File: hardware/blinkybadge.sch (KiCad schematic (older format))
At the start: 21 parts, among them IC101 ATMEGA8U2, P101 USB_OTG, P102 CONN_02X03, Q101 Q_PMOS_GDS, SW101 SPST, U101 ATECC508A, Y101 16MHz

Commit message: Layout complete
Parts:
- added R105: DNP, Resistors_SMD:R_0603, symbol R
- added W3: HWBE, Measurement_Points:Measurement_Point_Round-SMD-Pad_Small, symbol TEST_1P
- P102: footprint (none) -> lib:CONN_2.54mm_2x3_TP
- renumbered W3 to W4
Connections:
- net VCC: now also R105.1
- net at IC101.10 ((INT5/AIN3)PD4): now also C105.1, R104.2
- net at IC101.11 ((XCK/AIN4/PCINT12)PD5): now also C105.2
- net at IC101.13 ((~CTS~/~HWB~/AIN6/T0/INT7)PD7): now also R105.2, W3.1
- net at IC101.26 ((PCINT10)PC4): no longer C105.2
- now unconnected: IC101.5 ((PCINT11/AIN2)PC2)
- no-connect marks 2 -> 12
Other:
- moved on the sheet: C105, R104, W4
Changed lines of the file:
@@
 L C C105
 U 1 1 577EF93B
-P 7050 5150
-F 0 "C105" H 7075 5250 50  0000 L CNN
-F 1 "C" H 7075 5050 50  0000 L CNN
-F 2 "Capacitors_SMD:C_0603" H 7088 5000 50  0001 C CNN
-F 3 "" H 7050 5150 50  0000 C CNN
-	1    7050 5150
+P 7050 4650
+F 0 "C105" H 7075 4750 50  0000 L CNN
+F 1 "C" H 7075 4550 50  0000 L CNN
+F 2 "Capacitors_SMD:C_0603" H 7088 4500 50  0001 C CNN
+F 3 "" H 7050 4650 50  0000 C CNN
+	1    7050 4650
 	0    1    1    0
 $EndComp
@@
 L R R104
 U 1 1 577EF9C0
-P 7450 5050
-F 0 "R104" V 7530 5050 50  0000 C CNN
-F 1 "R" V 7450 5050 50  0000 C CNN
-F 2 "Resistors_SMD:R_0603" V 7380 5050 50  0001 C CNN
-F 3 "" H 7450 5050 50  0000 C CNN
-	1    7450 5050
+P 7450 4550
+F 0 "R104" V 7530 4550 50  0000 C CNN
+F 1 "R" V 7450 4550 50  0000 C CNN
+F 2 "Resistors_SMD:R_0603" V 7380 4550 50  0001 C CNN
+F 3 "" H 7450 4550 50  0000 C CNN
+	1    7450 4550
 	0    1    1    0
 $EndComp
@@
 F 0 "P102" H 7450 2850 50  0000 C CNN
 F 1 "CONN_02X03" H 7450 2450 50  0000 C CNN
-F 2 "" H 7450 1450 50  0001 C CNN
+F 2 "lib:CONN_2.54mm_2x3_TP" H 7450 1450 50  0001 C CNN
 F 3 "" H 7450 1450 50  0000 C CNN
 	1    7450 2650
@@
 	1600 2400 1600 2600
 Wire Wire Line
-	1500 2000 1950 2000
-Wire Wire Line
-	1950 2000 2300 2000
+	1500 2000 2300 2000
 Wire Wire Line
 	3350 2000 3000 2000
@@
 	5100 1600 5100 1700
 Wire Wire Line
-	1950 1600 4400 1600
-Wire Wire Line
-	4400 1600 5100 1600
-Wire Wire Line
-	5100 1600 5500 1600
+	1950 1600 5500 1600
 Wire Wire Line
 	1950 1600 1950 2000
@@
 Connection ~ 5100 1600
 Wire Wire Line
-	5300 2000 5500 2000
-Wire Wire Line
-	5500 2000 5700 2000
-Wire Wire Line
-	5700 1700 5700 2000
-Wire Wire Line
-	5700 2000 5700 2850
-Wire Wire Line
-	5700 2850 5700 2950
+	5300 2000 5700 2000
 Connection ~ 5500 2000
 Wire Wire Line
@@
 	4400 4550 4400 5000
 Wire Wire Line
-	4400 5300 4400 5350
-Wire Wire Line
-	4400 5350 4400 5400
+	4400 5300 4400 5400
 Wire Wire Line
 	4600 4950 4600 5350
@@
 Connection ~ 4400 5350
 Wire Wire Line
-	4000 4050 4200 4050
-Wire Wire Line
-	4200 4050 4400 4050
+	4000 4050 4400 4050
 Wire Wire Line
 	4400 3850 4600 3850
@@
 	4400 3750 4400 3850
 Wire Wire Line
-	4000 3750 4200 3750
-Wire Wire Line
-	4200 3750 4400 3750
+	4000 3750 4400 3750
 Wire Wire Line
 	4600 3950 4400 3950
@@
 	3700 3750 3550 3750
 Wire Wire Line
-	3550 3750 3550 4050
-Wire Wire Line
-	3550 4050 3550 4200
+	3550 3750 3550 4200
 Connection ~ 3550 4050
 Wire Wire Line
@@
 	8000 3750 8000 3850
 Wire Wire Line
-	7900 3650 8000 3650
-Wire Wire Line
 	8000 3650 8000 3550
 Wire Wire Line
-	4150 2850 4500 2850
-Wire Wire Line
-	4500 2850 5700 2850
-Wire Wire Line
-	4500 2850 4500 3750
-Wire Wire Line
-	4500 3750 4500 4650
+	5700 2850 4150 2850
+Wire Wire Line
+	4500 2850 4500 4650
 Wire Wire Line
 	4500 3750 4600 3750
@@
 	8950 4150 9100 4150
 Wire Wire Line
-	6800 5050 7250 5050
-Wire Wire Line
-	7250 5050 7300 5050
-Wire Wire Line
-	6800 5150 6900 5150
-Wire Wire Line
-	7200 5150 7250 5150
-Wire Wire Line
-	7250 5150 7250 5050
-Connection ~ 7250 5050
-Wire Wire Line
-	7600 5050 7850 5050
+	6800 4550 7300 4550
+Wire Wire Line
+	6800 4650 6900 4650
+Wire Wire Line
+	7200 4650 7250 4650
+Wire Wire Line
+	7250 4650 7250 4550
+Connection ~ 7250 4550
+Wire Wire Line
+	7600 4550 7850 4550
 Wire Wire Line
 	4600 2750 7200 2750
@@
 	6800 4450 6950 4450
 $Comp
-L TEST_1P W3
+L TEST_1P W4
 U 1 1 57805F3E
-P 7850 5050
-F 0 "W3" H 7850 5320 50  0000 C CNN
-F 1 "CAP_SENSE_BUTTON" H 7850 5250 50  0000 C CNN
-F 2 "Measurement_Points:Measurement_Point_Round-SMD-Pad_Small" H 8050 5050 50  0001 C CNN
-F 3 "" H 8050 5050 50  0000 C CNN
-	1    7850 5050
+P 7850 4550
+F 0 "W4" H 7850 4820 50  0000 C CNN
+F 1 "CAP_SENSE_BUTTON" H 7850 4750 50  0000 C CNN
+F 2 "Measurement_Points:Measurement_Point_Round-SMD-Pad_Small" H 8050 4550 50  0001 C CNN
+F 3 "" H 8050 4550 50  0000 C CNN
+	1    7850 4550
 	1    0    0    -1
 $EndComp
@@
 Text Label 4000 4850 0    60   ~ 0
 USBR_N
+$Comp
+L TEST_1P W3
+U 1 1 57845845
+P 7600 4850
+F 0 "W3" H 7600 5120 50  0000 C CNN
+F 1 "HWBE" H 7600 5050 50  0000 C CNN
+F 2 "Measurement_Points:Measurement_Point_Round-SMD-Pad_Small" H 7800 4850 50  0001 C CNN
+F 3 "" H 7800 4850 50  0000 C CNN
+	1    7600 4850
+	0    1    1    0
+$EndComp
+Wire Wire Line
+	6800 4850 7600 4850
+$Comp
+L R R105
+U 1 1 57846CBE
+P 7750 4650
+F 0 "R105" V 7830 4650 50  0000 C CNN
+F 1 "DNP" V 7750 4650 50  0000 C CNN
+F 2 "Resistors_SMD:R_0603" V 7680 4650 50  0001 C CNN
+F 3 "" H 7750 4650 50  0000 C CNN
+	1    7750 4650
+	0    1    1    0
+$EndComp
+Wire Wire Line
+	7600 4650 7450 4650
+Wire Wire Line
+	7450 4650 7450 4850
+Connection ~ 7450 4850
+Wire Wire Line
+	7900 4650 8000 4650
+Wire Wire Line
+	8000 4650 8000 4500
+$Comp
+L VCC #PWR013
+U 1 1 57846ECD
+P 8000 4500
+F 0 "#PWR013" H 8000 4350 50  0001 C CNN
+F 1 "VCC" H 8000 4650 50  0000 C CNN
+F 2 "" H 8000 4500 50  0000 C CNN
+F 3 "" H 8000 4500 50  0000 C CNN
+	1    8000 4500
+	1    0    0    -1
+$EndComp
+NoConn ~ 6800 3250
+NoConn ~ 6800 3850
+NoConn ~ 6800 3950
+NoConn ~ 6800 4250
+NoConn ~ 6800 5050
+NoConn ~ 6800 5150
+NoConn ~ 6800 5250
+NoConn ~ 6800 5350
+NoConn ~ 6800 5450
+NoConn ~ 6800 4750
+Wire Wire Line
+	7900 3650 8000 3650
+Wire Wire Line
+	5700 1700 5700 2950
 $EndSCHEMATC

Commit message: Add some layout tweaks
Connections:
- net STAT: now also IC101.12 ((~RTS~/AIN5/INT6)PD6)
- no-connect marks 12 -> 11
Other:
- moved on the sheet: C105, R104, R105, W3, W4
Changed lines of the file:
@@
 L C C105
 U 1 1 577EF93B
-P 7050 4650
-F 0 "C105" H 7075 4750 50  0000 L CNN
-F 1 "C" H 7075 4550 50  0000 L CNN
-F 2 "Capacitors_SMD:C_0603" H 7088 4500 50  0001 C CNN
-F 3 "" H 7050 4650 50  0000 C CNN
-	1    7050 4650
+P 7200 4650
+F 0 "C105" H 7225 4750 50  0000 L CNN
+F 1 "C" H 7225 4550 50  0000 L CNN
+F 2 "Capacitors_SMD:C_0603" H 7238 4500 50  0001 C CNN
+F 3 "" H 7200 4650 50  0000 C CNN
+	1    7200 4650
 	0    1    1    0
 $EndComp
@@
 L R R104
 U 1 1 577EF9C0
-P 7450 4550
-F 0 "R104" V 7530 4550 50  0000 C CNN
-F 1 "R" V 7450 4550 50  0000 C CNN
-F 2 "Resistors_SMD:R_0603" V 7380 4550 50  0001 C CNN
-F 3 "" H 7450 4550 50  0000 C CNN
-	1    7450 4550
+P 7600 4550
+F 0 "R104" V 7680 4550 50  0000 C CNN
+F 1 "R" V 7600 4550 50  0000 C CNN
+F 2 "Resistors_SMD:R_0603" V 7530 4550 50  0001 C CNN
+F 3 "" H 7600 4550 50  0000 C CNN
+	1    7600 4550
 	0    1    1    0
 $EndComp
@@
 	8950 4150 9100 4150
 Wire Wire Line
-	6800 4550 7300 4550
-Wire Wire Line
-	6800 4650 6900 4650
-Wire Wire Line
-	7200 4650 7250 4650
-Wire Wire Line
-	7250 4650 7250 4550
-Connection ~ 7250 4550
-Wire Wire Line
-	7600 4550 7850 4550
+	6800 4550 7450 4550
+Wire Wire Line
+	6800 4650 7050 4650
+Wire Wire Line
+	7350 4650 7400 4650
+Wire Wire Line
+	7400 4650 7400 4550
+Connection ~ 7400 4550
+Wire Wire Line
+	7750 4550 8000 4550
 Wire Wire Line
 	4600 2750 7200 2750
@@
 L TEST_1P W4
 U 1 1 57805F3E
-P 7850 4550
-F 0 "W4" H 7850 4820 50  0000 C CNN
-F 1 "CAP_SENSE_BUTTON" H 7850 4750 50  0000 C CNN
-F 2 "Measurement_Points:Measurement_Point_Round-SMD-Pad_Small" H 8050 4550 50  0001 C CNN
-F 3 "" H 8050 4550 50  0000 C CNN
-	1    7850 4550
+P 8000 4550
+F 0 "W4" H 8000 4820 50  0000 C CNN
+F 1 "CAP_SENSE_BUTTON" H 8000 4750 50  0000 C CNN
+F 2 "Measurement_Points:Measurement_Point_Round-SMD-Pad_Small" H 8200 4550 50  0001 C CNN
+F 3 "" H 8200 4550 50  0000 C CNN
+	1    8000 4550
 	1    0    0    -1
 $EndComp
@@
 L TEST_1P W3
 U 1 1 57845845
-P 7600 4850
-F 0 "W3" H 7600 5120 50  0000 C CNN
-F 1 "HWBE" H 7600 5050 50  0000 C CNN
-F 2 "Measurement_Points:Measurement_Point_Round-SMD-Pad_Small" H 7800 4850 50  0001 C CNN
-F 3 "" H 7800 4850 50  0000 C CNN
-	1    7600 4850
-	0    1    1    0
-$EndComp
-Wire Wire Line
-	6800 4850 7600 4850
+P 7750 4850
+F 0 "W3" H 7750 5120 50  0000 C CNN
+F 1 "HWBE" H 7750 5050 50  0000 C CNN
+F 2 "Measurement_Points:Measurement_Point_Round-SMD-Pad_Small" H 7950 4850 50  0001 C CNN
+F 3 "" H 7950 4850 50  0000 C CNN
+	1    7750 4850
+	0    1    1    0
+$EndComp
+Wire Wire Line
+	6800 4850 7750 4850
 $Comp
 L R R105
 U 1 1 57846CBE
-P 7750 4650
-F 0 "R105" V 7830 4650 50  0000 C CNN
-F 1 "DNP" V 7750 4650 50  0000 C CNN
-F 2 "Resistors_SMD:R_0603" V 7680 4650 50  0001 C CNN
-F 3 "" H 7750 4650 50  0000 C CNN
-	1    7750 4650
-	0    1    1    0
-$EndComp
-Wire Wire Line
-	7600 4650 7450 4650
-Wire Wire Line
-	7450 4650 7450 4850
-Connection ~ 7450 4850
-Wire Wire Line
-	7900 4650 8000 4650
-Wire Wire Line
-	8000 4650 8000 4500
+P 7900 4650
+F 0 "R105" V 7980 4650 50  0000 C CNN
+F 1 "DNP" V 7900 4650 50  0000 C CNN
+F 2 "Resistors_SMD:R_0603" V 7830 4650 50  0001 C CNN
+F 3 "" H 7900 4650 50  0000 C CNN
+	1    7900 4650
+	0    1    1    0
+$EndComp
+Wire Wire Line
+	7750 4650 7600 4650
+Wire Wire Line
+	7600 4650 7600 4850
+Connection ~ 7600 4850
+Wire Wire Line
+	8050 4650 8150 4650
+Wire Wire Line
+	8150 4650 8150 4500
 $Comp
 L VCC #PWR013
 U 1 1 57846ECD
-P 8000 4500
-F 0 "#PWR013" H 8000 4350 50  0001 C CNN
-F 1 "VCC" H 8000 4650 50  0000 C CNN
-F 2 "" H 8000 4500 50  0000 C CNN
-F 3 "" H 8000 4500 50  0000 C CNN
-	1    8000 4500
+P 8150 4500
+F 0 "#PWR013" H 8150 4350 50  0001 C CNN
+F 1 "VCC" H 8150 4650 50  0000 C CNN
+F 2 "" H 8150 4500 50  0000 C CNN
+F 3 "" H 8150 4500 50  0000 C CNN
+	1    8150 4500
 	1    0    0    -1
 $EndComp
@@
 NoConn ~ 6800 5350
 NoConn ~ 6800 5450
-NoConn ~ 6800 4750
 Wire Wire Line
 	7900 3650 8000 3650
 Wire Wire Line
 	5700 1700 5700 2950
+Wire Wire Line
+	6800 4750 7050 4750
+Text Label 6850 4750 0    60   ~ 0
+STAT
 $EndSCHEMATC

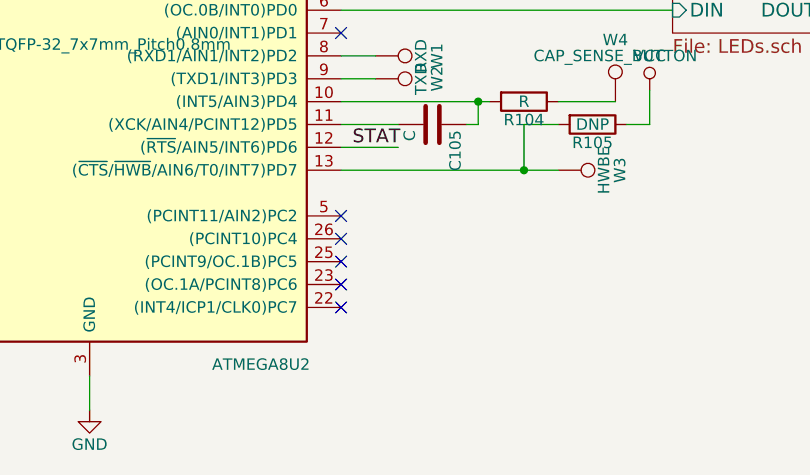
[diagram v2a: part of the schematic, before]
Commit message: Add footprints and the EURion constellations
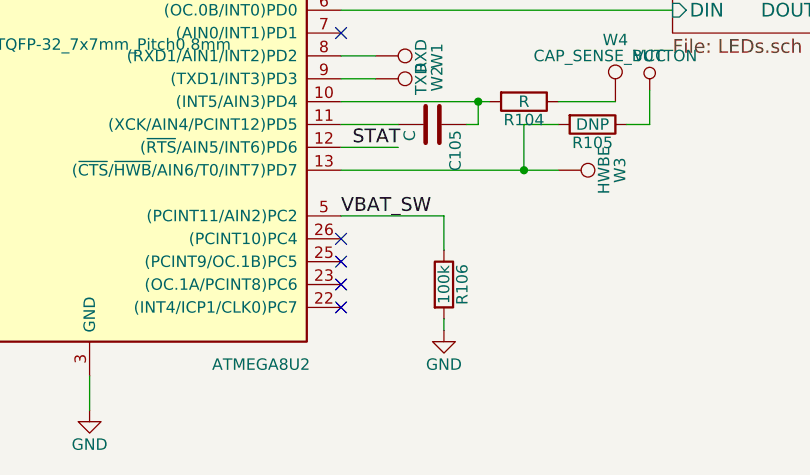
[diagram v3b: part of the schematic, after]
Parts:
- added R106: 100k, Resistors_SMD:R_0603, symbol R
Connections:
- net GND: now also R106.2
- net VBAT_SW: now also IC101.5 ((PCINT11/AIN2)PC2), R106.1
- no-connect marks 11 -> 10
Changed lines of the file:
@@
 NoConn ~ 6800 3950
 NoConn ~ 6800 4250
-NoConn ~ 6800 5050
 NoConn ~ 6800 5150
 NoConn ~ 6800 5250
@@
 Text Label 6850 4750 0    60   ~ 0
 STAT
+Wire Wire Line
+	6800 5050 7250 5050
+Text Label 6800 5050 0    60   ~ 0
+VBAT_SW
+Wire Wire Line
+	7250 5050 7250 5200
+$Comp
+L R R106
+U 1 1 578530AE
+P 7250 5350
+F 0 "R106" V 7330 5350 50  0000 C CNN
+F 1 "100k" V 7250 5350 50  0000 C CNN
+F 2 "Resistors_SMD:R_0603" V 7180 5350 50  0001 C CNN
+F 3 "" H 7250 5350 50  0000 C CNN
+	1    7250 5350
+	1    0    0    -1
+$EndComp
+$Comp
+L GND #PWR014
+U 1 1 5785312D
+P 7250 5550
+F 0 "#PWR014" H 7250 5300 50  0001 C CNN
+F 1 "GND" H 7250 5400 50  0000 C CNN
+F 2 "" H 7250 5550 50  0000 C CNN
+F 3 "" H 7250 5550 50  0000 C CNN
+	1    7250 5550
+	1    0    0    -1
+$EndComp
+Wire Wire Line
+	7250 5500 7250 5550
 $EndSCHEMATC

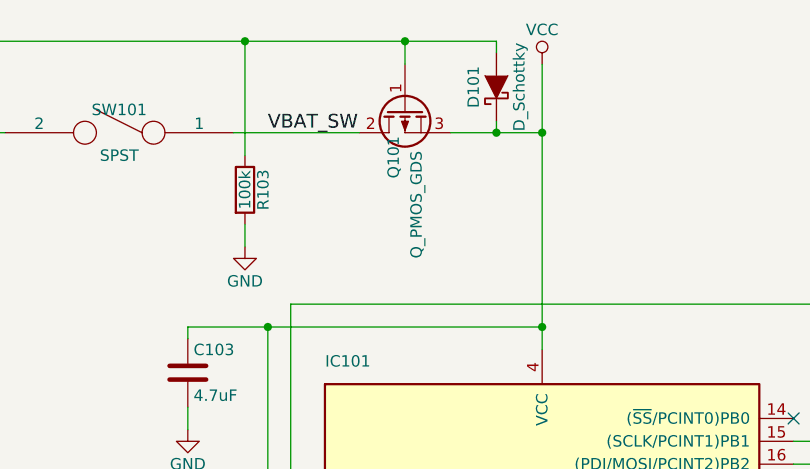
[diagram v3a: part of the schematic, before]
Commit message: Fix PMOS pinout
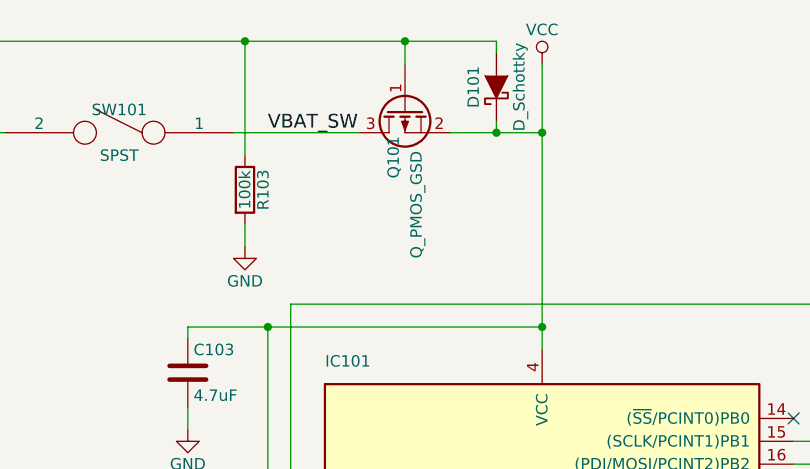
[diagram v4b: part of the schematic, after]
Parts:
- removed Q101: Q_PMOS_GDS, TO_SOT_Packages_SMD:SOT-23, symbol Q_PMOS_GDS
- added Q101: Q_PMOS_GSD, TO_SOT_Packages_SMD:SOT-23, symbol Q_PMOS_GSD
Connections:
- net Power/VUSB: now also Q101.1 (G)
- net VBAT_SW: now also Q101.3 (D)
- net VCC: now also Q101.2 (S)
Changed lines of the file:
@@
-$EndComp
-$Comp
-L Q_PMOS_GDS Q101
-U 1 1 577C833B
-P 5100 1900
-F 0 "Q101" H 5400 1950 50  0000 R CNN
-F 1 "Q_PMOS_GDS" H 5750 1850 50  0000 R CNN
-F 2 "TO_SOT_Packages_SMD:SOT-23" H 5300 2000 50  0001 C CNN
-F 3 "" H 5100 1900 50  0000 C CNN
-	1    5100 1900
-	0    -1   1    0
 $EndComp
 $Comp
@@
 Wire Wire Line
 	7250 5500 7250 5550
+$Comp
+L Q_PMOS_GSD Q101
+U 1 1 5790503C
+P 5100 1900
+F 0 "Q101" H 5400 1950 50  0000 R CNN
+F 1 "Q_PMOS_GSD" H 5750 1850 50  0000 R CNN
+F 2 "TO_SOT_Packages_SMD:SOT-23" H 5300 2000 50  0001 C CNN
+F 3 "" H 5100 1900 50  0000 C CNN
+	1    5100 1900
+	0    -1   1    0
+$EndComp
 $EndSCHEMATC

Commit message: Final tweaks
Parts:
- added R107, R108: DNP, Resistors_SMD:R_0603, symbol R
- IC101: value ATMEGA8U2 -> ATMEGA32U2
- R105: value DNP -> 100k
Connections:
- net LEDs/DIN: now also IC101.14 ((~SS~/PCINT0)PB0); no longer IC101.6 ((OC.0B/INT0)PD0)
- net VCC: now also R107.1, R108.1
- net at C105.1, IC101.10 ((INT5/AIN3)PD4): no longer R104.2
- net at C105.2, IC101.11 ((XCK/AIN4/PCINT12)PD5): now also R104.2
- net at IC101.18 ((T1/PCINT4)PB4), U101.5 (SDA): now also R107.2
- net at IC101.19 ((PCINT5)PB5), U101.6 (SCL): now also R108.2
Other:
- moved on the sheet: C105, C106, R104, R105, U101, W3, W4
